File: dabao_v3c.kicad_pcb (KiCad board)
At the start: 2 copper layers, 21 x 41 mm, 49 parts, among them J1 USB_C_Receptacle_USB2.0_16P, SW1 SW_Push, SW2 SW_Push, U1 baochip1x, U3 Baochip, U4 MT3406, U5 EMS4000RSW, U6 MT3406, Y2 48.000MHz

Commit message: update silkscreen and add step file
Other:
- board text added: "v3c 11/25"
- board text removed: "v3b 10/25"
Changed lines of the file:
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@@
 		)
 	)
-	(gr_text "v3b 10/25"
+	(gr_text "v3c 11/25"
 		(at 132 93.6 0)
 		(layer "B.SilkS")

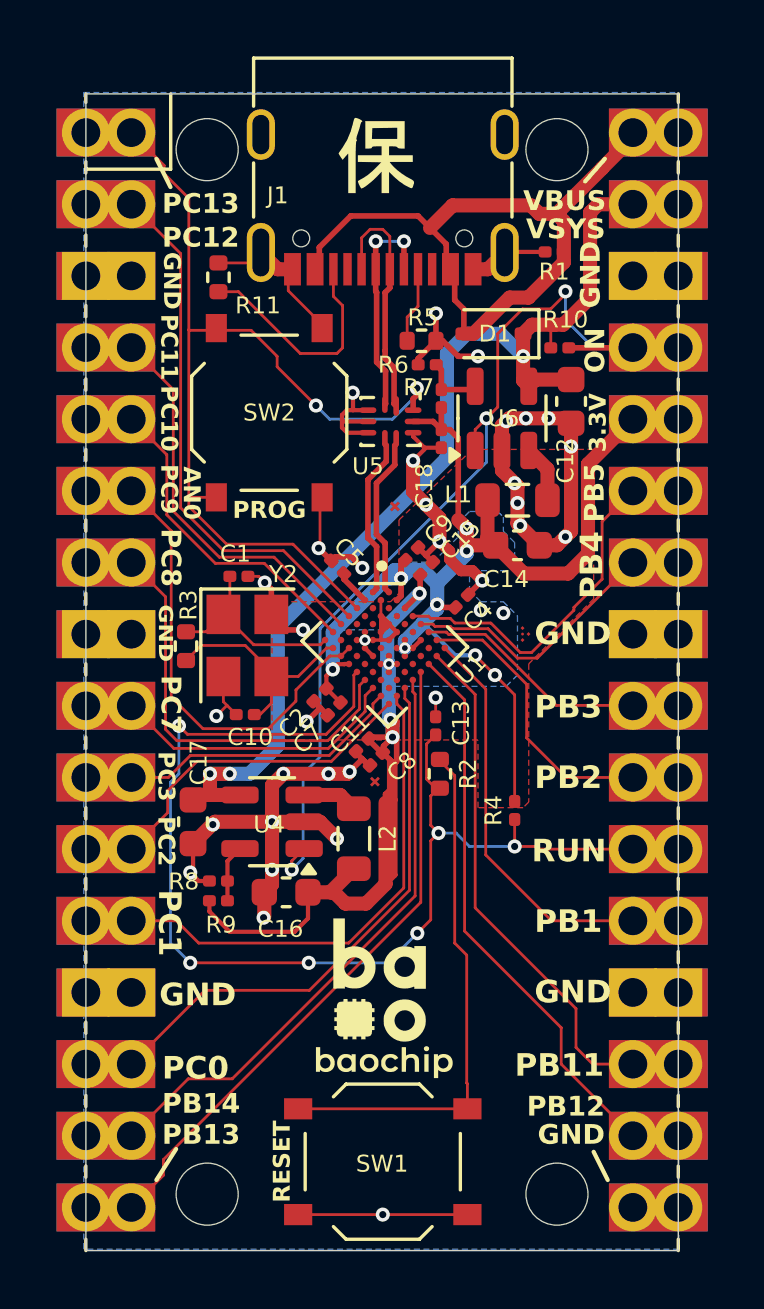
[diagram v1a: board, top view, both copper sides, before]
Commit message: update routing to latest rev
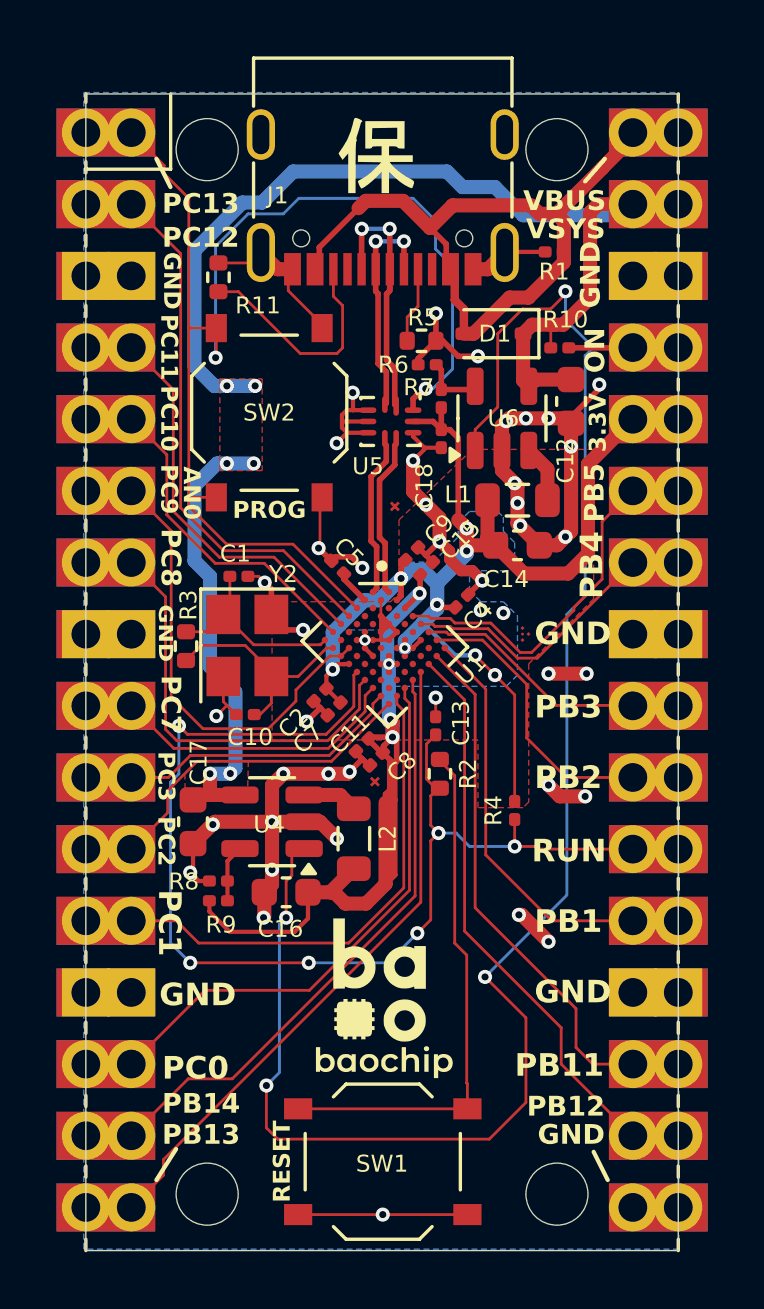
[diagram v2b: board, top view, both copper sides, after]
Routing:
- net /EN: track 33.1 -> 62.5 mm, vias 3 -> 4
- net /VSYS: track 37.4 -> 51.7 mm, vias 3 -> 6
- net /PC13: track 33.6 -> 45.2 mm
- net GND: track 75.8 -> 81.7 mm, vias 33 -> 41
- net +3.3V: track 44.0 -> 43.1 mm
- net /USBCONN_P: track 8.59 -> 8.88 mm, vias 0 -> 2
- added copper zone on F.Cu, net /VSYS
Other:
- board text added: "1.52mm"
- board text added: "1.6mm"
- board text removed: "0.7mm"
- board text removed: "0.8mm"

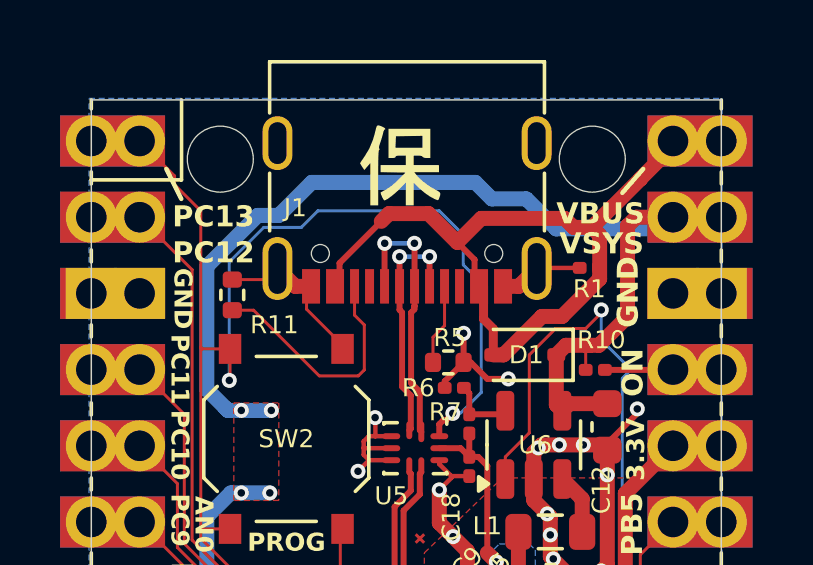
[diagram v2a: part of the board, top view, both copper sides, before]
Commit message: add usb pads on the back side
allows for pogo testing & also possibly SMT access to USB

board designers will have to exercise caution tho - 480Mbps won't
tolerate a lot of shenanigans in layout.
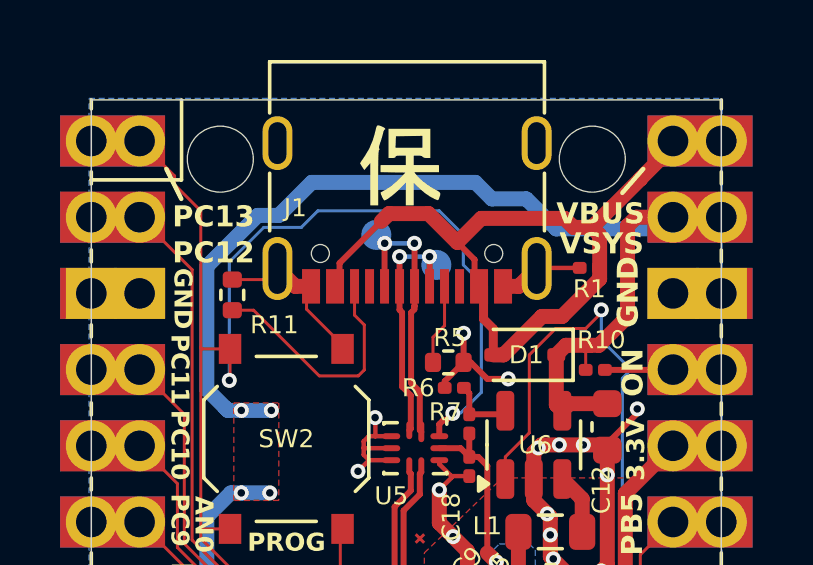
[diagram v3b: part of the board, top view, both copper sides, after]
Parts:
- added TP1: TestPoint, TestPoint:TestPoint_Pad_D1.0mm, B.Cu at (131.0, 64.0)
- added TP2: TestPoint, TestPoint:TestPoint_Pad_D1.0mm, B.Cu at (133.0, 65.0)
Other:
- board text added: "U+"
- board text added: "U-"
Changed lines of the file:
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@@
 		)
+	)
+	(footprint "TestPoint:TestPoint_Pad_D1.0mm"
+		(layer "B.Cu")
+		(at 131 64)
+		(descr "SMD pad as test Point, diameter 1.0mm")
+		(tags "test point SMD pad")
+		(property "Reference" "TP1"
+			(at 0 1.448 180)
+			(layer "B.SilkS")
+			(hide yes)
+			(effects
+				(font
+					(size 1 1)
+					(thickness 0.15)
+				)
+				(justify mirror)
+			)
+		)
+		(property "Value" "TestPoint"
+			(at 0 -1.55 180)
+			(layer "B.Fab")
+			(effects
+				(font
+					(size 1 1)
+					(thickness 0.15)
+				)
+				(justify mirror)
+			)
+		)
+		(property "Datasheet" "~"
+			(at 0 0 180)
+			(unlocked yes)
+			(layer "B.Fab")
+			(hide yes)
+			(effects
+				(font
+					(size 1.27 1.27)
+					(thickness 0.15)
+				)
+				(justify mirror)
+			)
+		)
+		(property "Description" "test point"
+			(at 0 0 180)
+			(unlocked yes)
+			(layer "B.Fab")
+			(hide yes)
+			(effects
+				(font
+					(size 1.27 1.27)
+					(thickness 0.15)
+				)
+				(justify mirror)
+			)
+		)
+		(property ki_fp_filters "Pin* Test*")
+		(sheetname "/")
+		(sheetfile "dabao_v3c.kicad_sch")
+		(attr exclude_from_pos_files exclude_from_bom)
+		(fp_circle
+			(center 0 0)
+			(end 0 -0.7)
+			(stroke
+				(width 0.12)
+				(type solid)
+			)
+			(fill no)
+			(layer "B.SilkS")
+		)
+		(fp_circle
+			(center 0 0)
+			(end 1 0)
+			(stroke
+				(width 0.05)
+				(type solid)
+			)
+			(fill no)
+			(layer "B.CrtYd")
+		)
+		(fp_text user "${REFERENCE}"
+			(at 0 1.45 180)
+			(layer "B.Fab")
+			(effects
+				(font
+					(size 1 1)
+					(thickness 0.15)
+				)
+				(justify mirror)
+			)
+		)
+		(pad "1" smd circle
+			(at 0 0)
+			(size 1 1)
+			(layers "B.Cu" "B.Mask")
+			(net 60 "/USBCONN_P")
+			(pinfunction "1")
+			(pintype "passive")
+		)
+		(embedded_fonts no)
 	)
 	(footprint "LOGO"
@@
 		(embedded_fonts no)
 	)
+	(footprint "TestPoint:TestPoint_Pad_D1.0mm"
+		(layer "B.Cu")
+		(at 133 65)
+		(descr "SMD pad as test Point, diameter 1.0mm")
+		(tags "test point SMD pad")
+		(property "Reference" "TP2"
+			(at 0 1.448 180)
+			(layer "B.SilkS")
+			(hide yes)
+			(effects
+				(font
+					(size 1 1)
+					(thickness 0.15)
+				)
+				(justify mirror)
+			)
+		)
+		(property "Value" "TestPoint"
+			(at 0 -1.55 180)
+			(layer "B.Fab")
+			(effects
+				(font
+					(size 1 1)
+					(thickness 0.15)
+				)
+				(justify mirror)
+			)
+		)
+		(property "Datasheet" "~"
+			(at 0 0 180)
+			(unlocked yes)
+			(layer "B.Fab")
+			(hide yes)
+			(effects
+				(font
+					(size 1.27 1.27)
+					(thickness 0.15)
+				)
+				(justify mirror)
+			)
+		)
+		(property "Description" "test point"
+			(at 0 0 180)
+			(unlocked yes)
+			(layer "B.Fab")
+			(hide yes)
+			(effects
+				(font
+					(size 1.27 1.27)
+					(thickness 0.15)
+				)
+				(justify mirror)
+			)
+		)
+		(property ki_fp_filters "Pin* Test*")
+		(sheetname "/")
+		(sheetfile "dabao_v3c.kicad_sch")
+		(attr exclude_from_pos_files exclude_from_bom)
+		(fp_circle
+			(center 0 0)
+			(end 0 -0.7)
+			(stroke
+				(width 0.12)
+				(type solid)
+			)
+			(fill no)
+			(layer "B.SilkS")
+		)
+		(fp_circle
+			(center 0 0)
+			(end 1 0)
+			(stroke
+				(width 0.05)
+				(type solid)
+			)
+			(fill no)
+			(layer "B.CrtYd")
+		)
+		(fp_text user "${REFERENCE}"
+			(at 0 1.45 180)
+			(layer "B.Fab")
+			(effects
+				(font
+					(size 1 1)
+					(thickness 0.15)
+				)
+				(justify mirror)
+			)
+		)
+		(pad "1" smd circle
+			(at 0 0)
+			(size 1 1)
+			(layers "B.Cu" "B.Mask")
+			(net 61 "/USBCONN_N")
+			(pinfunction "1")
+			(pintype "passive")
+		)
+		(embedded_fonts no)
+	)
 	(gr_line
 		(start 139.5 97)
@@
 		)
 	)
+	(gr_text "U+"
+		(at 131.67 63.07 0)
+		(layer "B.SilkS")
+		(effects
+			(font
+				(size 0.6 0.6)
+				(thickness 0.15)
+				(bold yes)
+			)
+			(justify left bottom mirror)
+		)
+	)
 	(gr_text "CERN\nOHL-W-2.0"
 		(at 132 97.8 0)
@@
 		)
 	)
+	(gr_text "U-"
+		(at 133.67 64.06 0)
+		(layer "B.SilkS")
+		(effects
+			(font
+				(size 0.6 0.6)
+				(thickness 0.15)
+				(bold yes)
+			)
+			(justify left bottom mirror)
+		)
+	)
